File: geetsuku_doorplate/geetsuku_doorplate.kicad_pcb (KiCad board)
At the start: 2 copper layers, 100 x 100 mm, 3 parts

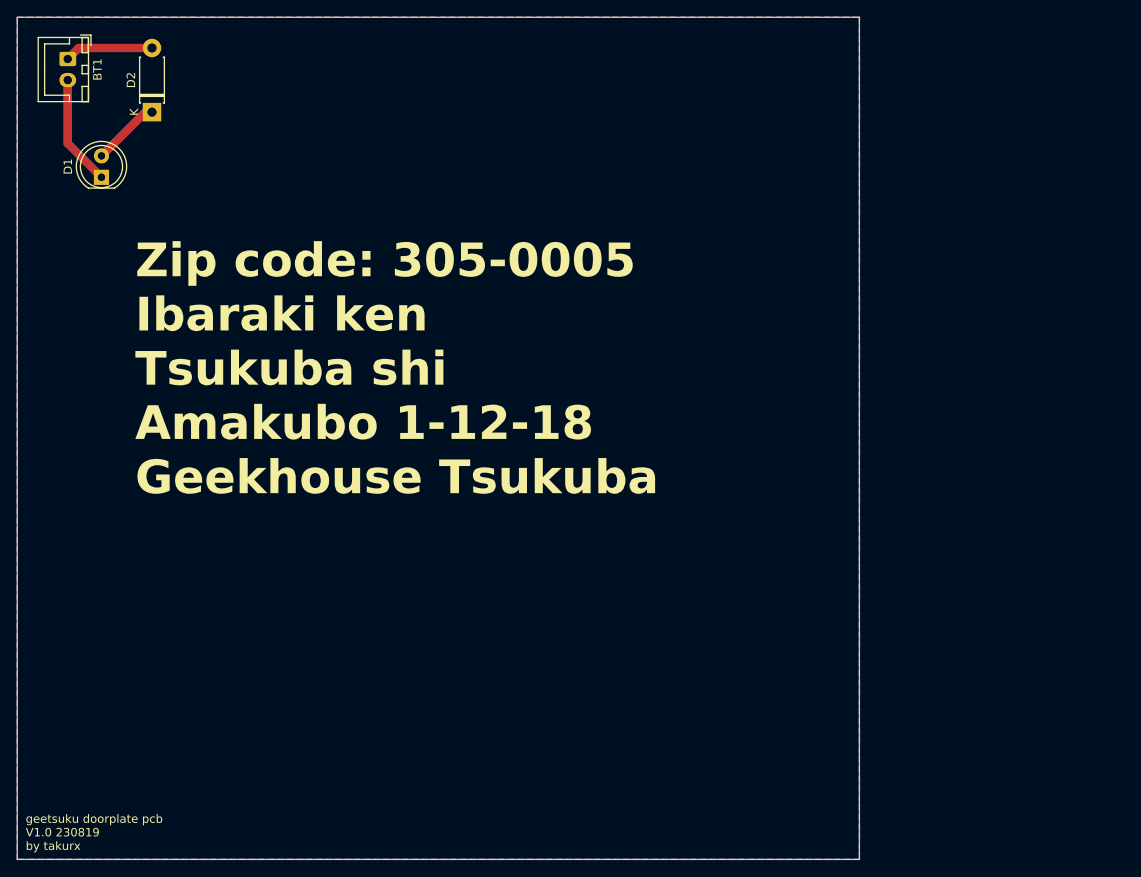
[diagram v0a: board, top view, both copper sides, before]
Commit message: add v1.2
1.1 add hole x4
1.2 change font, kicad font -> ubuntu with Bold
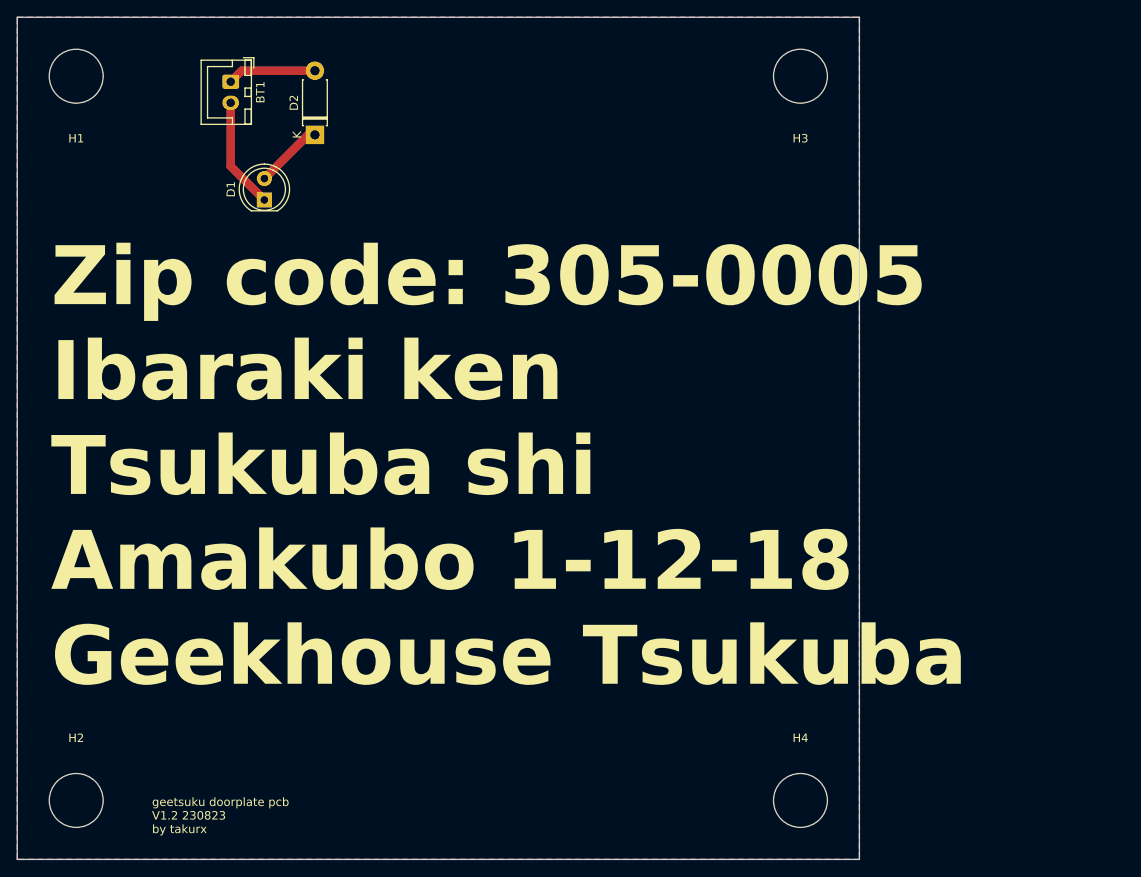
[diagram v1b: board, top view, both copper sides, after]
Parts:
- added H1: MountingHole, MountingHole:MountingHole_6.4mm_M6, F.Cu at (99.0, 64.0)
- added H2: MountingHole, MountingHole:MountingHole_6.4mm_M6, F.Cu at (99.0, 150.0)
- added H3: MountingHole, MountingHole:MountingHole_6.4mm_M6, F.Cu at (185.0, 64.0)
- added H4: MountingHole, MountingHole:MountingHole_6.4mm_M6, F.Cu at (185.0, 150.0)
- moved D2 19.5 mm to (127.3, 71.0)
- moved BT1 19.5 mm to (117.3, 64.7)
- moved D1 19.5 mm to (121.3, 78.7)
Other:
- board text added: "geetsuku doorplate pcb V1.2 230823 by takurx"
- board text removed: "geetsuku doorplate pcb V1.0 230819 by takurx"
